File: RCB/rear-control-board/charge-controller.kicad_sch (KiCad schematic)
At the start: 2 parts

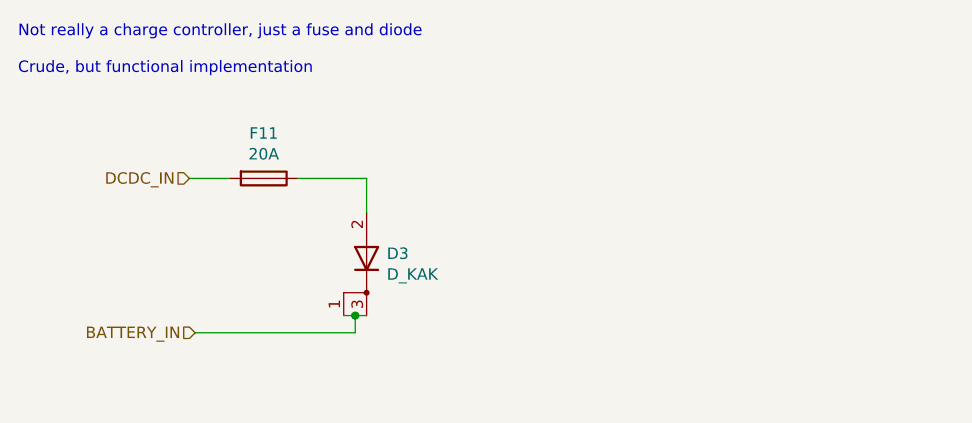
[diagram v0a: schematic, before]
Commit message: working on layout
Updating traces for RCB and organizing HVB
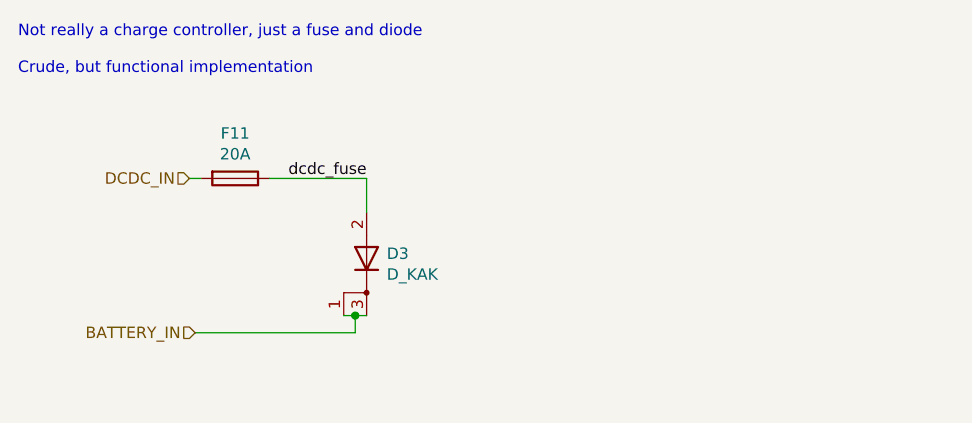
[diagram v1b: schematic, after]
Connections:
- net dcdc_fuse: now reaches D3.2 (A), F11.1
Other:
- moved on the sheet: F11
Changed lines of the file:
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@@
   (junction (at 117.475 97.79) (diameter 0) (color 0 0 0 0)
   )
-  (wire (pts (xy 111.125 82.55) (xy 118.745 82.55))
+  (wire (pts (xy 107.95 82.55) (xy 118.745 82.55))
     (stroke (width 0) (type default) (color 0 0 0 0))
   )
@@
     (stroke (width 0) (type default) (color 0 0 0 0))
   )
-  (wire (pts (xy 99.06 82.55) (xy 103.505 82.55))
+  (wire (pts (xy 99.06 82.55) (xy 100.33 82.55))
     (stroke (width 0) (type default) (color 0 0 0 0))
   )
@@
     (effects (font (size 1.27 1.27)) (justify left bottom))
   )
+  (label "dcdc_fuse" (at 118.745 82.55 180)
+    (effects (font (size 1.27 1.27)) (justify right bottom))
+  )
   (hierarchical_label "DCDC_IN" (shape input) (at 99.06 82.55 180)
     (effects (font (size 1.27 1.27)) (justify right))
@@
     (effects (font (size 1.27 1.27)) (justify right))
   )
-  (symbol (lib_id "Device:Fuse") (at 107.315 82.55 270) (unit 1)
+  (symbol (lib_id "Device:Fuse") (at 104.14 82.55 270) (unit 1)
     (in_bom yes) (on_board yes)
-    (property "Reference" "F11" (id 0) (at 107.315 77.5462 90))
-    (property "Value" "20A" (id 1) (at 107.315 79.8576 90))
-    (property "Footprint" "AERO_Footprints:Fuseholder_Blade_Mini_Keystone_3568" (id 2) (at 107.315 80.772 90)
+    (property "Reference" "F11" (id 0) (at 104.14 77.5462 90))
+    (property "Value" "20A" (id 1) (at 104.14 79.8576 90))
+    (property "Footprint" "AERO_Footprints:Fuseholder_Blade_Mini_Keystone_3568" (id 2) (at 104.14 80.772 90)
       (effects (font (size 1.27 1.27)) hide)
     )
-    (property "Datasheet" "~" (id 3) (at 107.315 82.55 0)
+    (property "Datasheet" "~" (id 3) (at 104.14 82.55 0)
       (effects (font (size 1.27 1.27)) hide)
     )

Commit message: willem review notes
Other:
- note added: "Add some currnet protection - Charge controller ic for protection"
- note added: "INA series chip to mointor current for VICOR. this is if we wanted to do MCU"
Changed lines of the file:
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@@
     (stroke (width 0) (type default) (color 0 0 0 0))
+  )
+  (text "Add some currnet protection\n - Charge controller ic for protection"
+    (at 107.95 107.315 0)
+    (effects (font (size 1.27 1.27)) (justify left bottom))
   )
   (text "Not really a charge controller, just a fuse and diode\n\nCrude, but functional implementation"
@@
     (effects (font (size 1.27 1.27)) (justify left bottom))
   )
+  (text "INA series chip to mointor current\nfor VICOR. this is if we wanted to do \nMCU"
+    (at 138.43 94.615 0)
+    (effects (font (size 1.27 1.27)) (justify left bottom))
+  )
